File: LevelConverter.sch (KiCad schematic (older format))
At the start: 3 parts, among them Q5 BSS138

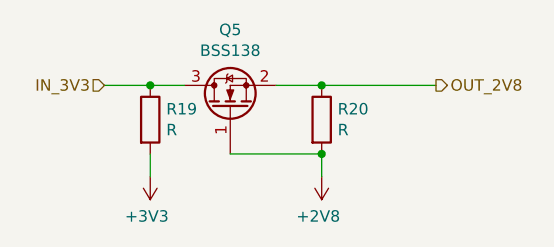
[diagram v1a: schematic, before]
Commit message: Added resistors values
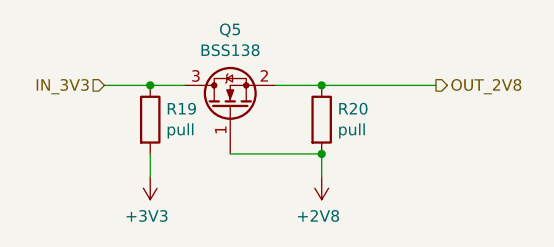
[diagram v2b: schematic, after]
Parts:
- R19, R20: value R -> pull
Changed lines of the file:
@@
 AR Path="/5BBEFA89/5BBEDD94" Ref="R14"  Part="1"
 F 0 "R20" H 4470 3196 50  0000 L CNN
-F 1 "R" H 4470 3105 50  0000 L CNN
+F 1 "pull" H 4470 3105 50  0000 L CNN
 F 2 "Resistor_SMD:R_0805_2012Metric_Pad1.15x1.40mm_HandSolder" V 4330 3150 50  0001 C CNN
 F 3 "~" H 4400 3150 50  0001 C CNN
@@
 AR Path="/5BBEFA89/5BBEDDA3" Ref="R13"  Part="1"
 F 0 "R19" H 3720 3196 50  0000 L CNN
-F 1 "R" H 3720 3105 50  0000 L CNN
+F 1 "pull" H 3720 3105 50  0000 L CNN
 F 2 "Resistor_SMD:R_0805_2012Metric_Pad1.15x1.40mm_HandSolder" V 3580 3150 50  0001 C CNN
 F 3 "~" H 3650 3150 50  0001 C CNN
